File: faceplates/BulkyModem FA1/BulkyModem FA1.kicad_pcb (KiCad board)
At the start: 2 copper layers, 100 x 100 mm, 7 parts, among them M1 Mounting, M2 Mounting, M3 Mounting, M4 Mounting

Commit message: Alternate panel designs
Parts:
- removed REF***: KiCad-Logo2_6mm_SilkScreen, Symbols:KiCad-Logo2_6mm_SilkScreen
- G***: moved to F.Cu
- REF**: footprint BulkyMIDI-32:PWR_Specification -> BulkyModem:PWR_Specification_Single
- moved G*** 39.3 mm to (120.2, 143.9), turned to 0 degrees
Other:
- outline, holes or cut-outs redrawn
- board text removed: "BulkyModem Faceplate FA1 github.com/tebl"

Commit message: Exported files
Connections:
- M1 pad 1: Net-(M1-Pad1) -> unconnected-(M1-Pin_1-Pad1)
- M2 pad 1: Net-(M1-Pad1) -> unconnected-(M2-Pin_1-Pad1)
- M3 pad 1: Net-(M1-Pad1) -> unconnected-(M3-Pin_1-Pad1)
- M4 pad 1: Net-(M1-Pad1) -> unconnected-(M4-Pin_1-Pad1)
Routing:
- removed copper zone on F.Cu, net Net-(M1-Pad1)
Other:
- net class Default removed
- net class Power removed
- board text added: "WayWayWay"

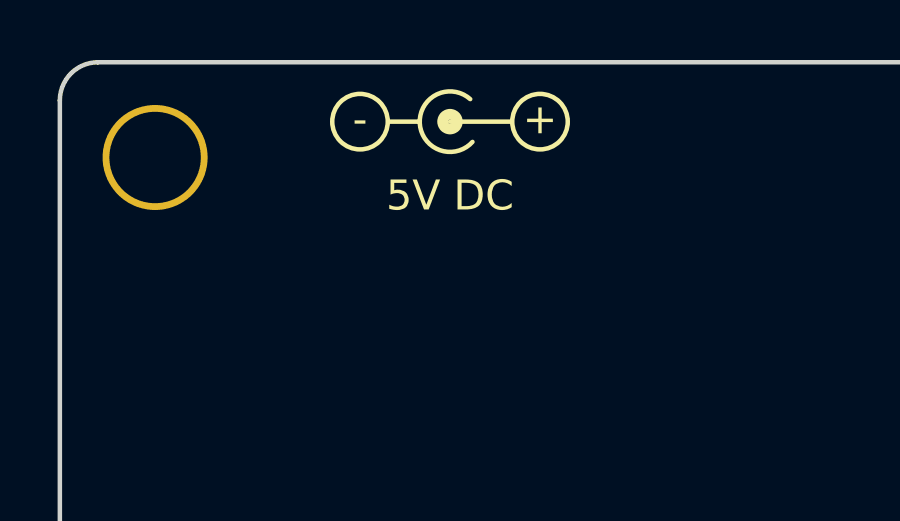
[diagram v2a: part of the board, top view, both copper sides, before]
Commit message: Move PS/2 port to the back with some caveats, basically needs a custom top panel
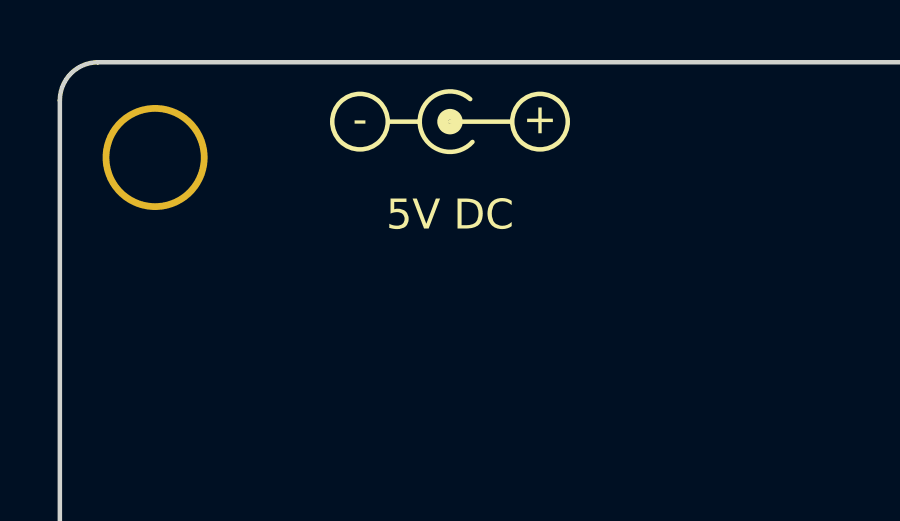
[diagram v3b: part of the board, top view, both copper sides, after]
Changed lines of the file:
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@@
 	)
 	(gr_text "5V DC"
-		(at 83.185 59.055 0)
+		(at 83.185 59.69 0)
 		(layer "F.SilkS")
 		(effects
 			(font
+				(face "C64 Pro")
 				(size 1 1)
 				(thickness 0.15)
 			)
 		)
+		(render_cache "5V DC" 0
+			(polygon
+				(pts
+					(xy 80.206702 60.105) (xy 80.206702 59.929877) (xy 80.034756 59.929877) (xy 80.034756 59.75793)
+					(xy 80.384756 59.75793) (xy 80.384756 59.929877) (xy 80.732069 59.929877) (xy 80.732069 59.404755)
+					(xy 80.034756 59.404755) (xy 80.034756 58.885739) (xy 81.082069 58.885739) (xy 81.082069 59.060861)
+					(xy 80.384756 59.060861) (xy 80.384756 59.229633) (xy 80.910122 59.229633) (xy 80.910122 59.398405)
+					(xy 81.082069 59.398405) (xy 81.082069 59.929877) (xy 80.910122 59.929877) (xy 80.910122 60.105)
+				)
+			)
+			(polygon
+				(pts
+					(xy 81.613297 60.105) (xy 81.613297 59.933053) (xy 81.431825 59.933053) (xy 81.431825 59.761106)
+					(xy 81.259878 59.761106) (xy 81.259878 58.885739) (xy 81.609878 58.885739) (xy 81.609878 59.761106)
+					(xy 81.963297 59.761106) (xy 81.963297 58.885739) (xy 82.307191 58.885739) (xy 82.307191 59.761106)
+					(xy 82.135244 59.761106) (xy 82.135244 59.933053) (xy 81.963297 59.933053) (xy 81.963297 60.105)
+				)
+			)
+			(polygon
+				(pts
+					(xy 84.585 59.057686) (xy 84.760366 59.057686) (xy 84.760366 59.229633) (xy 84.932313 59.229633)
+					(xy 84.932313 59.761106) (xy 84.760366 59.761106) (xy 84.760366 59.933053) (xy 84.585 59.933053)
+					(xy 84.585 60.105) (xy 83.885 60.105) (xy 83.885 59.929877) (xy 84.235 59.929877) (xy 84.410366 59.929877)
+					(xy 84.410366 59.761106) (xy 84.585 59.761106) (xy 84.585 59.229633) (xy 84.410366 59.229633) (xy 84.410366 59.060861)
+					(xy 84.235 59.060861) (xy 84.235 59.929877) (xy 83.885 59.929877) (xy 83.885 58.885739) (xy 84.585 58.885739)
+				)
+			)
+			(polygon
+				(pts
+					(xy 85.282069 60.105) (xy 85.282069 59.929877) (xy 85.110122 59.929877) (xy 85.110122 59.057686)
+					(xy 85.282069 59.057686) (xy 85.282069 58.885739) (xy 85.985488 58.885739) (xy 85.985488 59.057686)
+					(xy 86.157435 59.057686) (xy 86.157435 59.232808) (xy 85.807435 59.232808) (xy 85.807435 59.060861)
+					(xy 85.460122 59.060861) (xy 85.460122 59.929877) (xy 85.807435 59.929877) (xy 85.807435 59.75793)
+					(xy 86.157435 59.75793) (xy 86.157435 59.929877) (xy 85.985488 59.929877) (xy 85.985488 60.105)
+				)
+			)
+		)
